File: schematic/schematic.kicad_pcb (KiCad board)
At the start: 2 copper layers, 43.2 x 17.8 mm, 23 parts, among them J1 Analog, J2 Digital, U1 74HC595

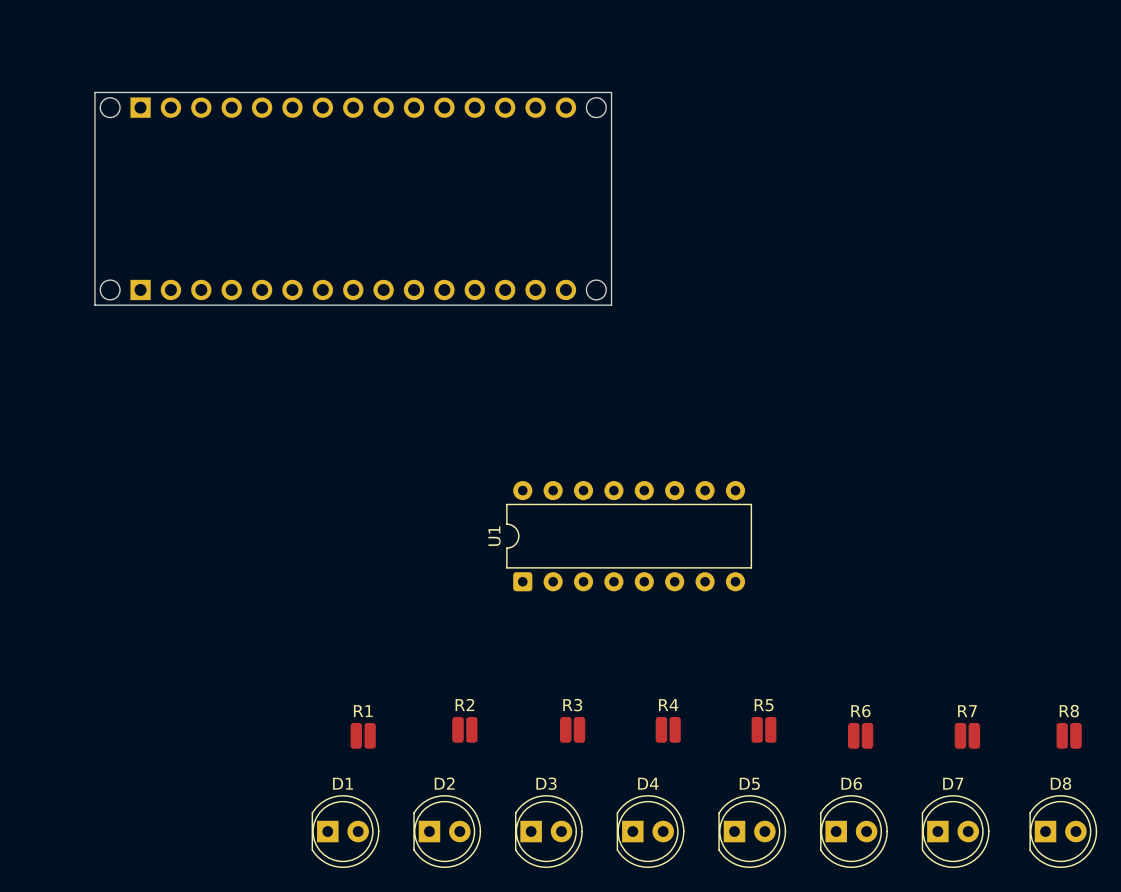
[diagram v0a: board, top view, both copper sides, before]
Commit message: Update schematic and swap pins for simplification
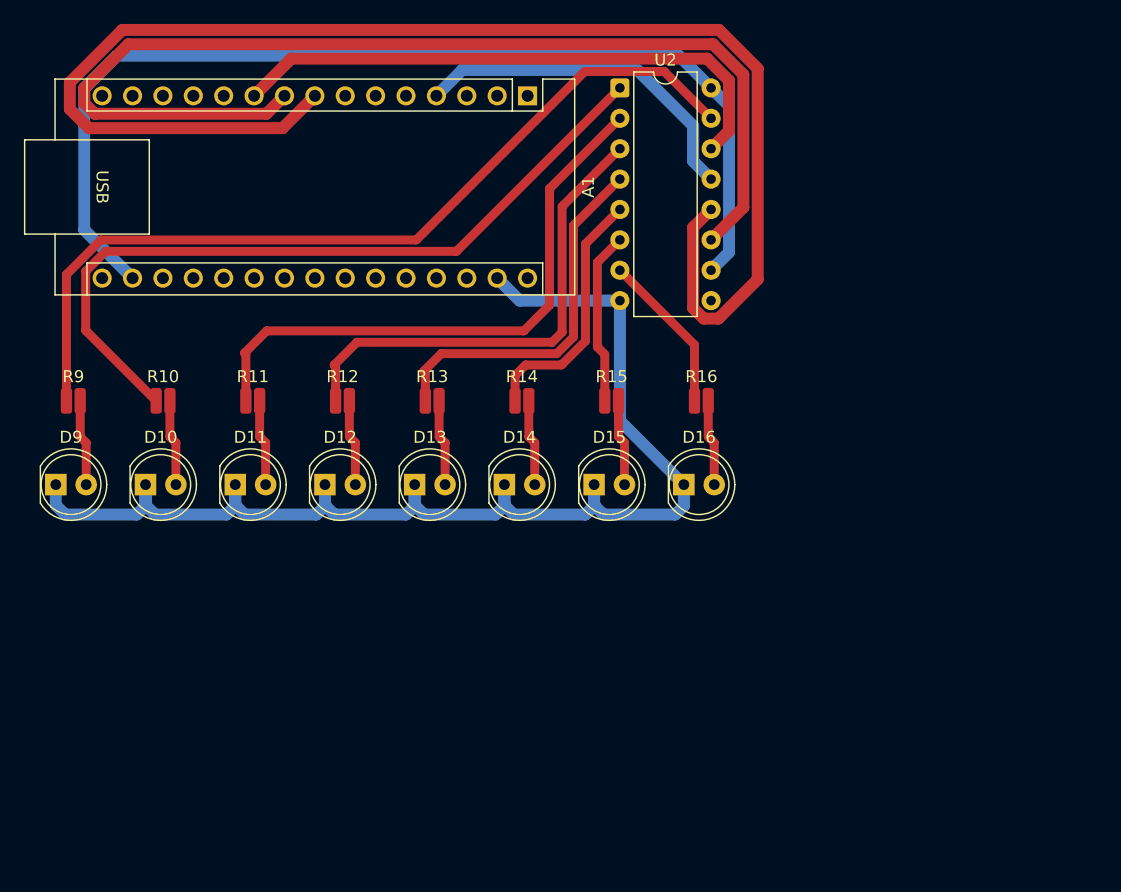
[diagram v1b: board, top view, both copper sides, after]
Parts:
- removed D1, D2, D3, D4, D5, D6, D7, D8: LED_Small, LED_THT:LED_D5.0mm
- removed J1: Analog, Connector_PinHeader_2.54mm:PinHeader_1x15_P2.54mm_Vertical
- removed J2: Digital, Connector_PinHeader_2.54mm:PinHeader_1x15_P2.54mm_Vertical
- removed MH1, MH2, MH3, MH4: MountingHole_65mil, Arduino_MountingHole:MountingHole_65mil
- removed R1, R2, R3, R4, R5, R6, R7, R8: 220, Resistor_SMD:R_0508_1220Metric
- removed U1: 74HC595, Package_DIP:DIP-16_W7.62mm
- added A1: Arduino_Nano_ESP32, Module:Arduino_Nano, F.Cu at (136.2, 82.5)
- added D10: LED_Small, LED_THT:LED_D5.0mm, F.Cu at (104.2, 115.0)
- added D11: LED_Small, LED_THT:LED_D5.0mm, F.Cu at (111.7, 115.0)
- added D12: LED_Small, LED_THT:LED_D5.0mm, F.Cu at (119.2, 115.0)
- added D13: LED_Small, LED_THT:LED_D5.0mm, F.Cu at (126.7, 115.0)
- added D14: LED_Small, LED_THT:LED_D5.0mm, F.Cu at (134.2, 115.0)
- added D15: LED_Small, LED_THT:LED_D5.0mm, F.Cu at (141.7, 115.0)
- added D16: LED_Small, LED_THT:LED_D5.0mm, F.Cu at (149.2, 115.0)
- added D9: LED_Small, LED_THT:LED_D5.0mm, F.Cu at (96.7, 115.0)
- added R10: 220, Resistor_SMD:R_0508_1220Metric, F.Cu at (105.7, 108.0)
- added R11: 220, Resistor_SMD:R_0508_1220Metric, F.Cu at (113.2, 108.0)
- added R12: 220, Resistor_SMD:R_0508_1220Metric, F.Cu at (120.7, 108.0)
- added R13: 220, Resistor_SMD:R_0508_1220Metric, F.Cu at (128.2, 108.0)
- added R14: 220, Resistor_SMD:R_0508_1220Metric, F.Cu at (135.7, 108.0)
- added R15: 220, Resistor_SMD:R_0508_1220Metric, F.Cu at (143.2, 108.0)
- added R16: 220, Resistor_SMD:R_0508_1220Metric, F.Cu at (150.7, 108.0)
- added R9: 220, Resistor_SMD:R_0508_1220Metric, F.Cu at (98.2, 108.0)
- added U2: 74HC595, Package_DIP:DIP-16_W7.62mm, F.Cu at (143.9, 81.8)
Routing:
- net Net-(D10-K): track 0.00 -> 139.3 mm
- net Net-(A1-D5): track 0.00 -> 118.8 mm
- net Net-(A1-D6): track 0.00 -> 91.6 mm
- net Net-(A1-3V3): track 0.00 -> 88.7 mm
- net Net-(U2-QA): track 0.00 -> 73.1 mm
- net Net-(U2-QB): track 0.00 -> 64.3 mm
- net Net-(U2-QC): track 0.00 -> 49.3 mm
- net Net-(A1-D7): track 0.00 -> 48.1 mm
- net Net-(U2-QD): track 0.00 -> 40.6 mm
- net Net-(U2-QE): track 0.00 -> 31.0 mm
- net Net-(U2-QF): track 0.00 -> 21.4 mm
- net Net-(U2-QG): track 0.00 -> 14.5 mm
- net Net-(U2-QH): track 0.00 -> 13.5 mm
- net Net-(D9-A): track 0.00 -> 7.21 mm
- net Net-(D16-A): track 0.00 -> 7.21 mm
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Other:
- board outline removed
- board text removed: "ICSP"
- board text removed: "USB Mini-B"

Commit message: Fix PCB board setup
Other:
- rule pad_to_mask_clearance: 0 -> 0.1
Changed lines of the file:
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@@
 				(type "Bottom Silk Screen")
 			)
-			(copper_finish "None")
+			(copper_finish "HAL lead-free")
 			(dielectric_constraints no)
 		)
-		(pad_to_mask_clearance 0)
+		(pad_to_mask_clearance 0.1)
+		(solder_mask_min_width 0.1)
 		(allow_soldermask_bridges_in_footprints no)
 		(tenting
